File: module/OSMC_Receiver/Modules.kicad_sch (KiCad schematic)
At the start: 44 parts, among them U2 LTC4317, U5 LTC4317, U6 LTC4317, U7 LTC4317

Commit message: update
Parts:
- R6: value 182k -> 102k
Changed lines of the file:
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@@
 			)
 		)
-		(property "Value" "182k"
+		(property "Value" "102k"
 			(at 17.272 135.89 0)
 			(effects

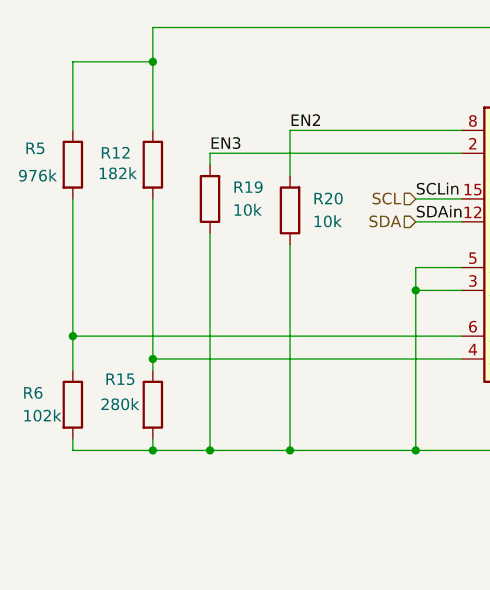
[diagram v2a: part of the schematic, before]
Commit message: update resistor value
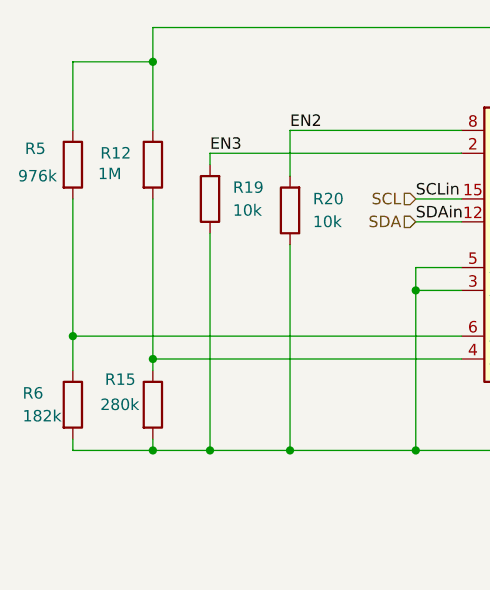
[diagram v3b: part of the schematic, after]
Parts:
- R12: value 182k -> 1M
- R6: value 102k -> 182k
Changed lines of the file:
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@@
 			)
 		)
-		(property "Value" "182k"
+		(property "Value" "1M"
 			(at 25.654 108.966 0)
 			(effects
@@
 			)
 		)
-		(property "Value" "102k"
+		(property "Value" "182k"
 			(at 17.272 135.89 0)
 			(effects
